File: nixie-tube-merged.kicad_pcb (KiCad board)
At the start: 2 copper layers, 99.8 x 97.5 mm, 0 parts

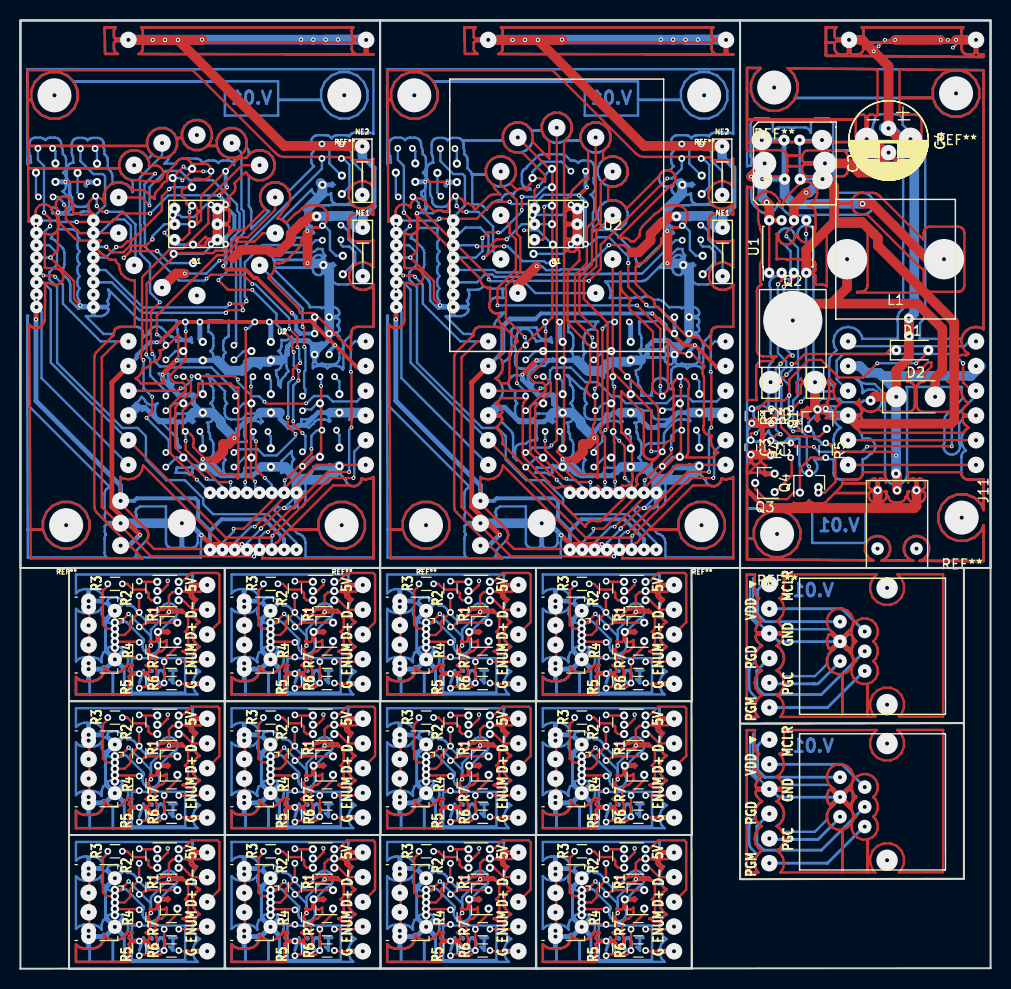
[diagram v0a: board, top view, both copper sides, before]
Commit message: combined all into nixie-tube-merged
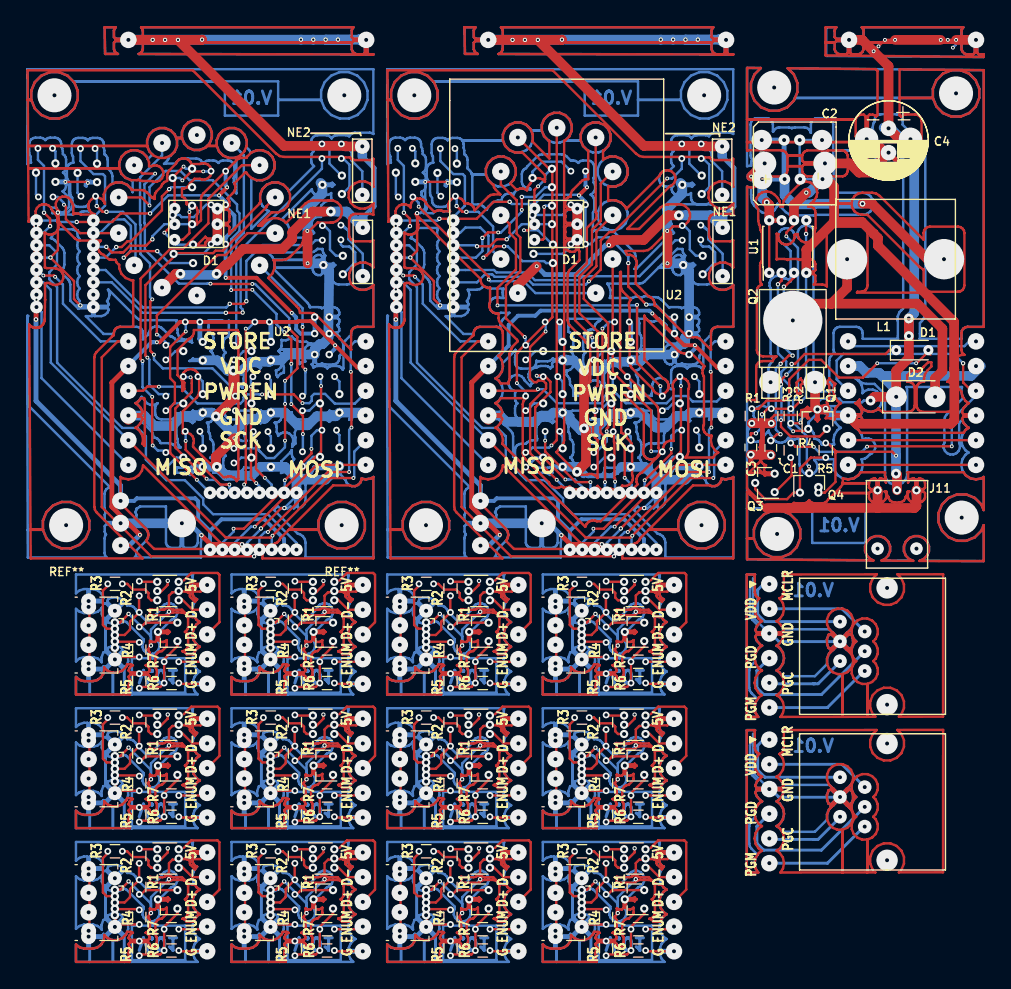
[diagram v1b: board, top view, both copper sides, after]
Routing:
- net 0: track 0.00 -> 12497.1 mm
- net (no net): track 12493.0 -> 0.00 mm, vias 1260 -> 1253
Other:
- board outline removed
- net class Default removed

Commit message: move outline to f and b silk
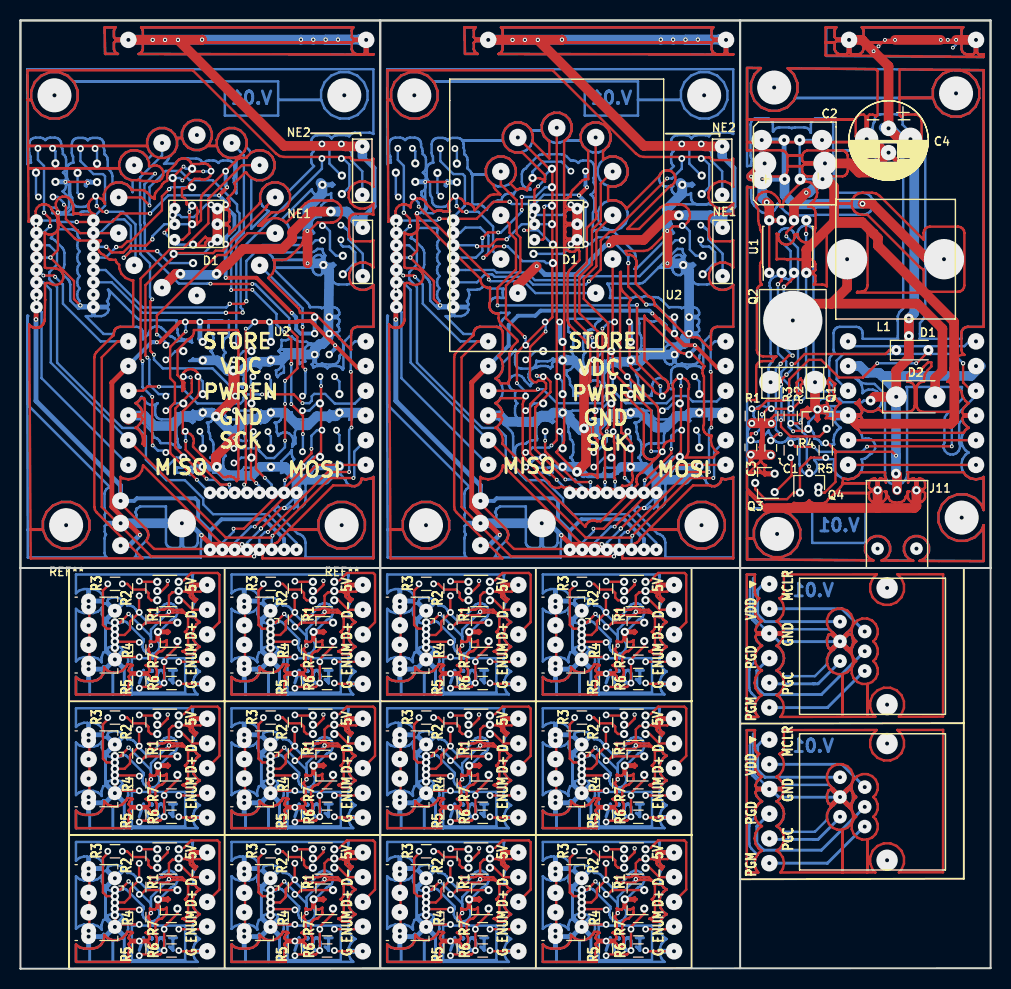
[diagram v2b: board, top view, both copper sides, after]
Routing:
- net 0: track 12497.1 -> 0.00 mm
- net (no net): track 0.00 -> 12497.1 mm
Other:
- board outline added: 99.8 x 97.5 mm
- net class Default added: clearance 0.2, trace_width 0.25, via_dia 0.6, via_drill 0.4

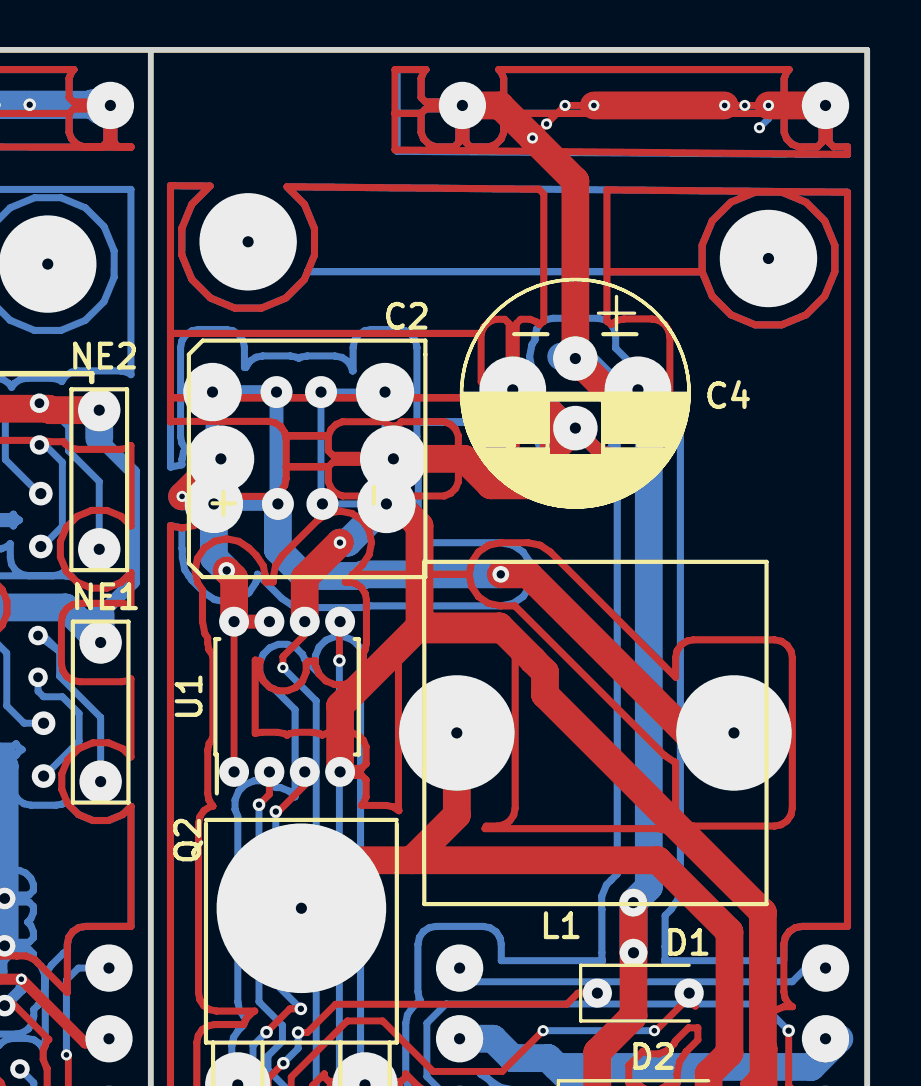
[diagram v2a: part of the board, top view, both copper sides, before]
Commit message: added panelizer folder project and panelized result
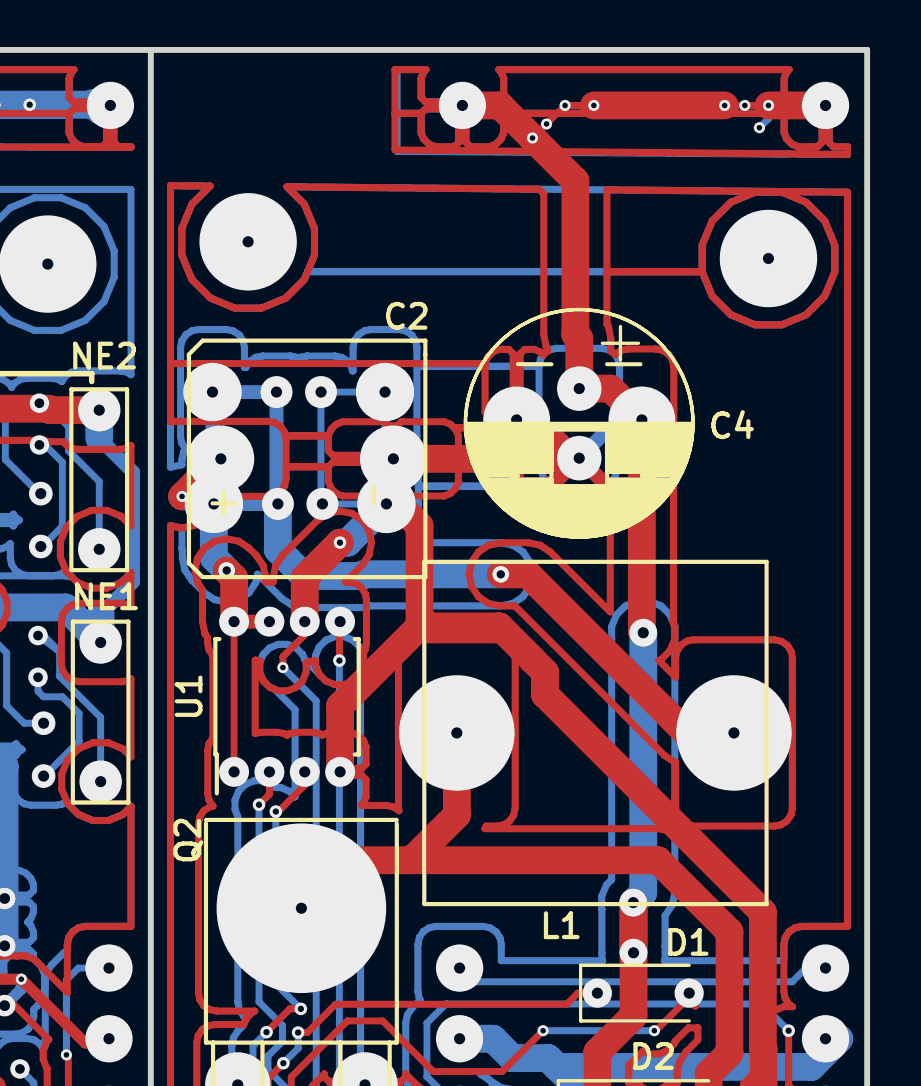
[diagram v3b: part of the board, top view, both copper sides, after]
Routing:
- net (no net): track 12497.1 -> 12472.3 mm, vias 1253 -> 1254
